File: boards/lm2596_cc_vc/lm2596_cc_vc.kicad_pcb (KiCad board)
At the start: 2 copper layers, 72.4 x 61.1 mm, 21 parts, among them J1 Vin, J2 Conn_Coaxial, J3 external_on/off, J4 Vout, Q1 pchannel, Q2 nchannel, U2 LM2596T-ADJ

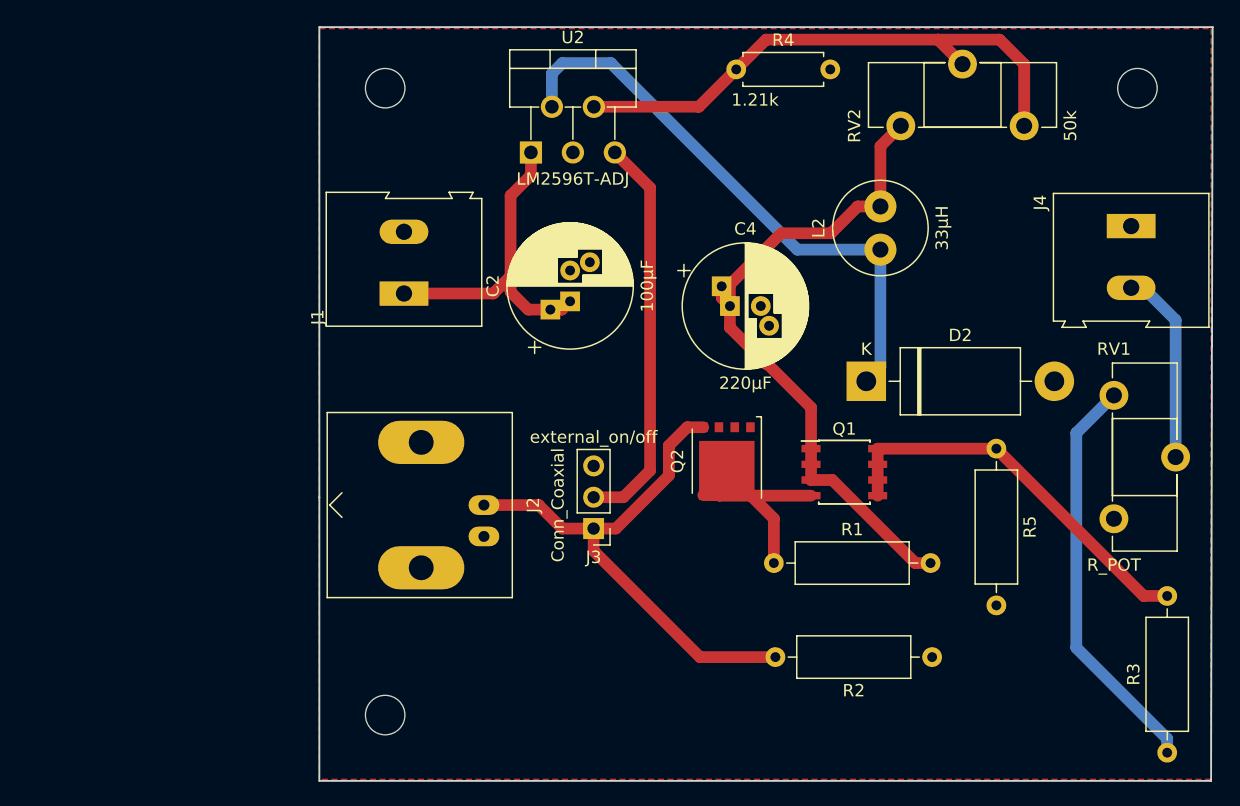
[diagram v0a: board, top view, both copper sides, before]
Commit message: added silk information to board
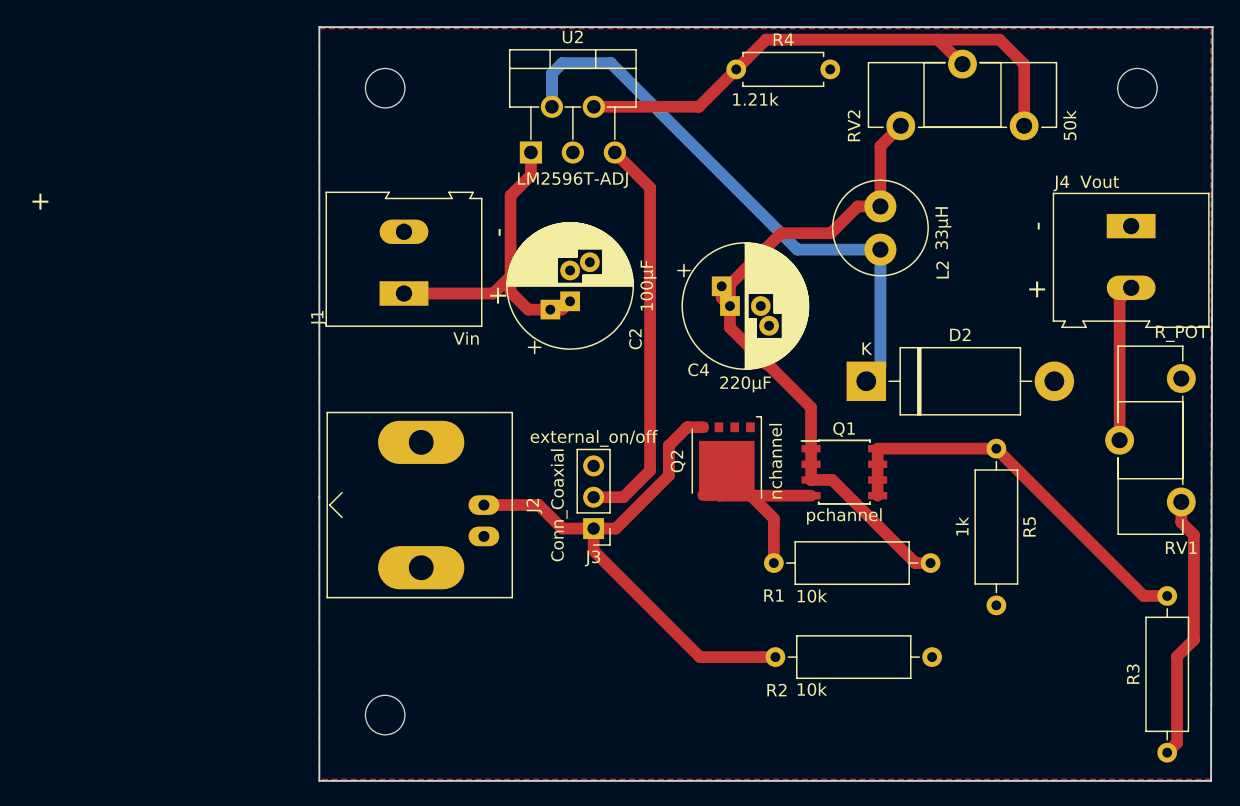
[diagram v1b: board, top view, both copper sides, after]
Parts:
- moved RV1 10.2 mm to (114.3, 105.8), turned to 180 degrees
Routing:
- net Net-(R3-Pad1): track 33.3 -> 21.6 mm
- net Net-(J4-Pad2): track 15.8 -> 13.7 mm
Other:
- board text added: "+"
- board text added: "-"
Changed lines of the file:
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@@
   (general
     (thickness 1.6)
-    (drawings 6)
-    (tracks 75)
+    (drawings 11)
+    (tracks 77)
     (zones 0)
     (modules 21)
@@
     (descr "CP, Radial series, Radial, pin pitch=2.50mm 5.00mm, , diameter=10mm, Electrolytic Capacitor")
     (tags "CP Radial series Radial pin pitch 2.50mm 5.00mm  diameter 10mm Electrolytic Capacitor")
-    (fp_text reference C2 (at 1.25 -6.25 90) (layer F.SilkS)
+    (fp_text reference C2 (at -3.048 5.334 90) (layer F.SilkS)
       (effects (font (size 1 1) (thickness 0.15)))
     )
@@
     (descr "CP, Radial series, Radial, pin pitch=2.50mm 5.00mm, , diameter=10mm, Electrolytic Capacitor")
     (tags "CP Radial series Radial pin pitch 2.50mm 5.00mm  diameter 10mm Electrolytic Capacitor")
-    (fp_text reference C4 (at 1.25 -6.25) (layer F.SilkS)
+    (fp_text reference C4 (at -2.54 5.207) (layer F.SilkS)
       (effects (font (size 1 1) (thickness 0.15)))
     )
@@
     (descr "Inductor, Radial series, Radial, pin pitch=3.50mm, , diameter=7.5mm, Fastron, 07P, http://www.fastrongroup.com/image-show/39/07P.pdf?type=Complete-DataSheet&productType=series")
     (tags "Inductor Radial series Radial pin pitch 3.50mm  diameter 7.5mm Fastron 07P")
-    (fp_text reference L2 (at 1.75 -5 90) (layer F.SilkS)
+    (fp_text reference L2 (at -1.651 5.08 90) (layer F.SilkS)
       (effects (font (size 1 1) (thickness 0.15)))
     )
@@
   )
   (module Potentiometer_THT:Potentiometer_Piher_PT-15-H25_Horizontal (layer F.Cu)
-    (at 108.839 97.155)
+    (at 114.3 105.791 180)
     (descr "Potentiometer, horizontal, Piher PT-15-H25, http://www.piher-nacesa.com/pdf/14-PT15v03.pdf")
     (tags "Potentiometer horizontal Piher PT-15-H25")
-    (fp_text reference RV1 (at 0 -3.75) (layer F.SilkS)
-      (effects (font (size 1 1) (thickness 0.15)))
-    )
-    (fp_text value R_POT (at 0 13.75) (layer F.SilkS)
-      (effects (font (size 1 1) (thickness 0.15)))
-    )
-    (fp_text user %R (at 2.5 5) (layer F.Fab)
+    (fp_text reference RV1 (at 0 -3.75 180) (layer F.SilkS)
+      (effects (font (size 1 1) (thickness 0.15)))
+    )
+    (fp_text value R_POT (at 0 13.75 180) (layer F.SilkS)
+      (effects (font (size 1 1) (thickness 0.15)))
+    )
+    (fp_text user %R (at 2.5 5 180) (layer F.Fab)
       (effects (font (size 1 1) (thickness 0.15)))
     )
@@
     (fp_line (start 5 12.5) (end 0 12.5) (layer F.Fab) (width 0.1))
     (fp_line (start 5 -2.5) (end 5 12.5) (layer F.Fab) (width 0.1))
-    (pad 1 thru_hole circle (at 0 0) (size 2.34 2.34) (drill 1.3) (layers *.Cu *.Mask)
+    (pad 1 thru_hole circle (at 0 0 180) (size 2.34 2.34) (drill 1.3) (layers *.Cu *.Mask)
       (net 10 "Net-(R3-Pad1)"))
-    (pad 2 thru_hole circle (at 5 5) (size 2.34 2.34) (drill 1.3) (layers *.Cu *.Mask)
+    (pad 2 thru_hole circle (at 5 5 180) (size 2.34 2.34) (drill 1.3) (layers *.Cu *.Mask)
       (net 7 "Net-(J4-Pad2)"))
-    (pad 3 thru_hole circle (at 0 10) (size 2.34 2.34) (drill 1.3) (layers *.Cu *.Mask))
+    (pad 3 thru_hole circle (at 0 10 180) (size 2.34 2.34) (drill 1.3) (layers *.Cu *.Mask))
     (model ${KISYS3DMOD}/Potentiometer_THT.3dshapes/Potentiometer_Piher_PT-15-H25_Horizontal.wrl
       (at (xyz 0 0 0))
@@
       (effects (font (size 1 1) (thickness 0.15)))
     )
-    (fp_text value Vin (at 2.78 7.75 90) (layer F.Fab)
+    (fp_text value Vin (at -3.683 5.08 180) (layer F.SilkS)
       (effects (font (size 1 1) (thickness 0.15)))
     )
@@
     (descr "Altech AK300 terminal block, pitch 5.0mm, 45 degree angled, see http://www.mouser.com/ds/2/16/PCBMETRC-24178.pdf")
     (tags "Altech AK300 terminal block pitch 5.0mm")
-    (fp_text reference J4 (at -1.905 7.366 270) (layer F.SilkS)
-      (effects (font (size 1 1) (thickness 0.15)))
-    )
-    (fp_text value Vout (at 2.78 7.75 270) (layer F.Fab)
+    (fp_text reference J4 (at -3.556 5.588) (layer F.SilkS)
+      (effects (font (size 1 1) (thickness 0.15)))
+    )
+    (fp_text value Vout (at -3.556 2.54) (layer F.SilkS)
       (effects (font (size 1 1) (thickness 0.15)))
     )
@@
       (effects (font (size 1 1) (thickness 0.15)))
     )
-    (fp_text value pchannel (at 0 3.5) (layer F.Fab)
+    (fp_text value pchannel (at 0 3.5) (layer F.SilkS)
       (effects (font (size 1 1) (thickness 0.15)))
     )
@@
       (effects (font (size 1 1) (thickness 0.15)))
     )
-    (fp_text value nchannel (at 0 -4 270) (layer F.Fab)
+    (fp_text value nchannel (at 0 -4 270) (layer F.SilkS)
       (effects (font (size 1 1) (thickness 0.15)))
     )
@@
     (descr "Resistor, Axial_DIN0309 series, Axial, Horizontal, pin pitch=12.7mm, 0.5W = 1/2W, length*diameter=9*3.2mm^2, http://cdn-reichelt.de/documents/datenblatt/B400/1_4W%23YAG.pdf")
     (tags "Resistor Axial_DIN0309 series Axial Horizontal pin pitch 12.7mm 0.5W = 1/2W length 9mm diameter 3.2mm")
-    (fp_text reference R1 (at 6.35 -2.72) (layer F.SilkS)
-      (effects (font (size 1 1) (thickness 0.15)))
-    )
-    (fp_text value 10k (at 6.35 2.72) (layer F.Fab)
+    (fp_text reference R1 (at 0 2.667) (layer F.SilkS)
+      (effects (font (size 1 1) (thickness 0.15)))
+    )
+    (fp_text value 10k (at 3.048 2.72) (layer F.SilkS)
       (effects (font (size 1 1) (thickness 0.15)))
     )
@@
     (descr "Resistor, Axial_DIN0309 series, Axial, Horizontal, pin pitch=12.7mm, 0.5W = 1/2W, length*diameter=9*3.2mm^2, http://cdn-reichelt.de/documents/datenblatt/B400/1_4W%23YAG.pdf")
     (tags "Resistor Axial_DIN0309 series Axial Horizontal pin pitch 12.7mm 0.5W = 1/2W length 9mm diameter 3.2mm")
-    (fp_text reference R2 (at 6.35 -2.72 180) (layer F.SilkS)
-      (effects (font (size 1 1) (thickness 0.15)))
-    )
-    (fp_text value 10k (at 6.35 2.72 180) (layer F.Fab)
+    (fp_text reference R2 (at 12.573 -2.72 180) (layer F.SilkS)
+      (effects (font (size 1 1) (thickness 0.15)))
+    )
+    (fp_text value 10k (at 9.779 -2.667 180) (layer F.SilkS)
       (effects (font (size 1 1) (thickness 0.15)))
     )
@@
       (effects (font (size 1 1) (thickness 0.15)))
     )
-    (fp_text value 1k (at 6.35 2.72 270) (layer F.Fab)
+    (fp_text value 1k (at 6.35 2.72 270) (layer F.SilkS)
       (effects (font (size 1 1) (thickness 0.15)))
     )
@@
     )
     (pad 1 np_thru_hole circle (at 0 0) (size 3.2 3.2) (drill 3.2) (layers *.Cu *.Mask))
+  )
+  (gr_text - (at 102.616 83.439 90) (layer F.SilkS)
+    (effects (font (size 1.5 1.5) (thickness 0.3)))
+  )
+  (gr_text - (at 58.928 83.947 90) (layer F.SilkS)
+    (effects (font (size 1.5 1.5) (thickness 0.3)))
+  )
+  (gr_text + (at 21.844 81.407) (layer F.SilkS)
+    (effects (font (size 1.5 1.5) (thickness 0.3)))
+  )
+  (gr_text + (at 102.616 88.519) (layer F.SilkS)
+    (effects (font (size 1.5 1.5) (thickness 0.3)))
+  )
+  (gr_text + (at 58.928 89.027) (layer F.SilkS)
+    (effects (font (size 1.5 1.5) (thickness 0.3)))
   )
   (target plus (at 49.784 123.063) (size 5) (width 0.15) (layer Edge.Cuts))
@@
   (segment (start 71.247 80.322) (end 71.247 103.251) (width 0.95) (layer F.Cu) (net 6))
   (segment (start 111.226 88.439) (end 110.236 88.439) (width 0.95) (layer B.Cu) (net 7))
-  (segment (start 113.839 91.052) (end 111.226 88.439) (width 0.95) (layer B.Cu) (net 7))
-  (segment (start 113.839 102.155) (end 113.839 91.052) (width 0.95) (layer B.Cu) (net 7))
+  (segment (start 109.3 89.375) (end 110.236 88.439) (width 0.95) (layer F.Cu) (net 7))
+  (segment (start 109.3 100.791) (end 109.3 89.375) (width 0.95) (layer F.Cu) (net 7))
   (segment (start 76.874 105.283) (end 76.83 105.239) (width 0.95) (layer F.Cu) (net 8))
   (segment (start 84.295 105.283) (end 76.874 105.283) (width 0.95) (layer F.Cu) (net 8))
@@
   (segment (start 111.252 113.411) (end 113.157 113.411) (width 0.95) (layer F.Cu) (net 9))
   (segment (start 99.314 101.473) (end 111.252 113.411) (width 0.95) (layer F.Cu) (net 9))
-  (segment (start 113.157 124.97963) (end 105.791 117.61363) (width 0.95) (layer B.Cu) (net 10))
-  (segment (start 113.157 126.111) (end 113.157 124.97963) (width 0.95) (layer B.Cu) (net 10))
-  (segment (start 105.791 100.203) (end 108.839 97.155) (width 0.95) (layer B.Cu) (net 10))
-  (segment (start 105.791 117.61363) (end 105.791 100.203) (width 0.95) (layer B.Cu) (net 10))
+  (segment (start 113.956999 125.311001) (end 113.956999 118.326001) (width 0.95) (layer F.Cu) (net 10))
+  (segment (start 113.157 126.111) (end 113.956999 125.311001) (width 0.95) (layer F.Cu) (net 10))
+  (segment (start 113.956999 118.326001) (end 115.316 116.967) (width 0.95) (layer F.Cu) (net 10))
+  (segment (start 114.3 107.445629) (end 114.3 105.791) (width 0.95) (layer F.Cu) (net 10))
+  (segment (start 115.316 108.461629) (end 114.3 107.445629) (width 0.95) (layer F.Cu) (net 10))
+  (segment (start 115.316 116.967) (end 115.316 108.461629) (width 0.95) (layer F.Cu) (net 10))
   (segment (start 75.201 73.77) (end 78.232 70.739) (width 0.95) (layer F.Cu) (net 11))
   (segment (start 66.695 73.77) (end 75.201 73.77) (width 0.95) (layer F.Cu) (net 11))
@@
     (connect_pads (clearance 0.508))
     (min_thickness 0.254)
-    (fill yes (arc_segments 16) (thermal_gap 0.508) (thermal_bridge_width 0.508))
+    (fill (arc_segments 16) (thermal_gap 0.508) (thermal_bridge_width 0.508))
     (polygon
       (pts
